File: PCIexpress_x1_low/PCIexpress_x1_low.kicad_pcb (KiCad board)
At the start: 6 copper layers, 167.7 x 68.9 mm, 29 parts, among them J1 PCIexpress_bracket, J2 PCIexpress_x1, J3 87832-1420, J4 PMOD_Host_Conn_02x06, J5 PMOD_Host_Conn_02x06, J6 PMOD_Host_Conn_02x06, U1 XC7A50T-CSG325, U2 LTM4643EY_PBF, U3 MX25L3233FM1

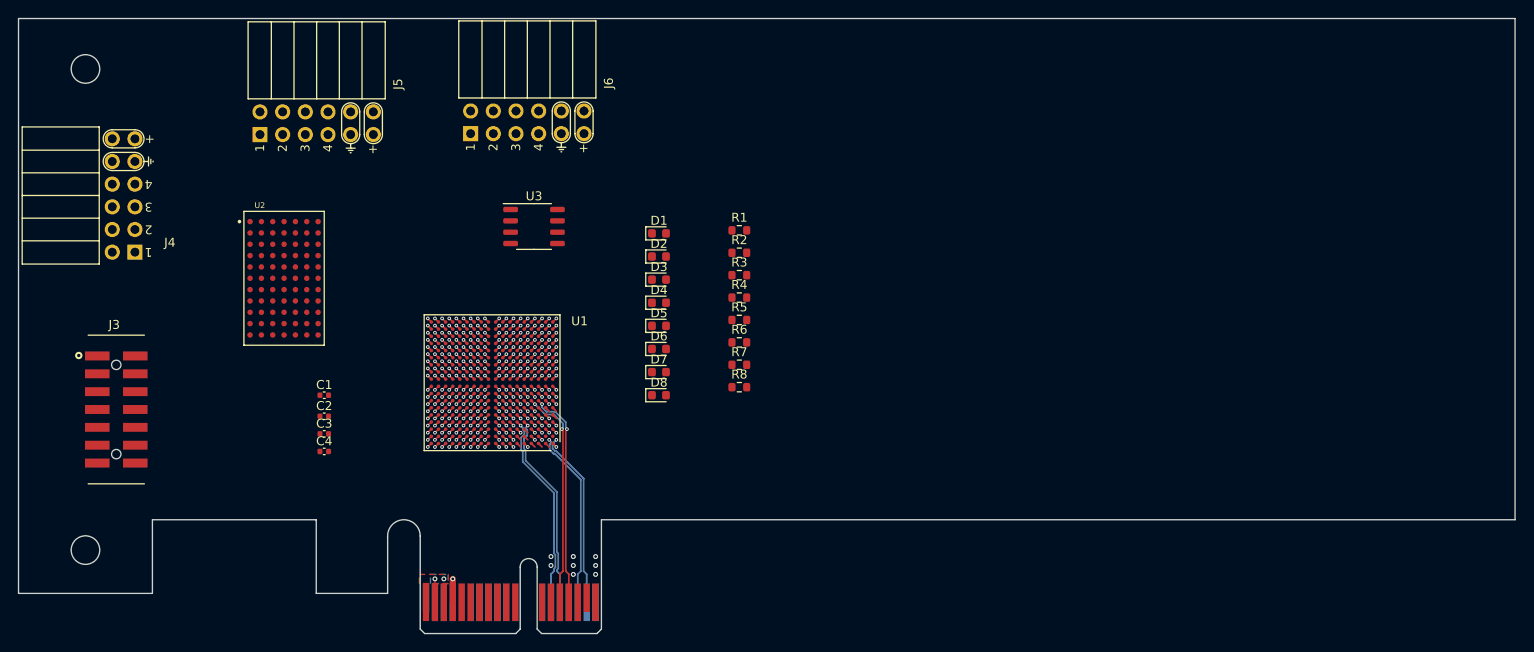
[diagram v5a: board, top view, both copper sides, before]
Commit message: using hierarchal sheets
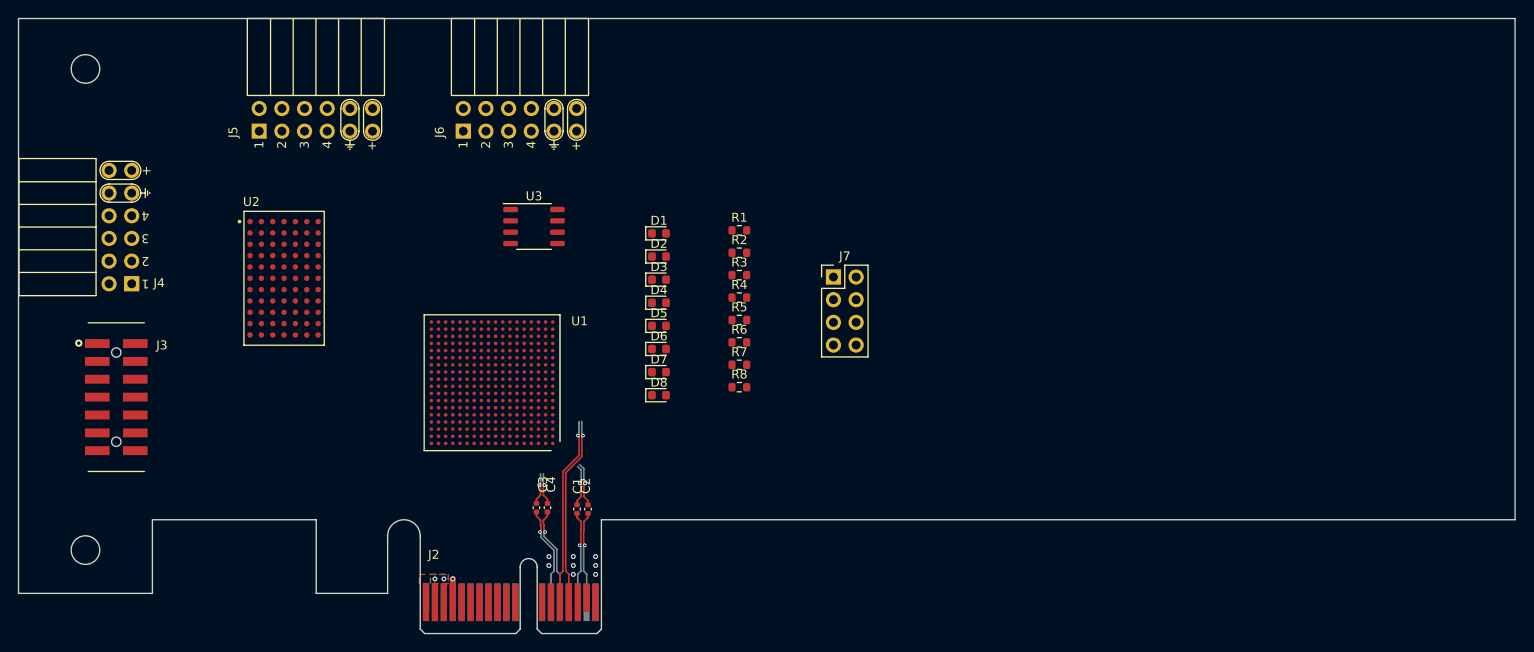
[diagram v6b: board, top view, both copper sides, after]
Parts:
- added J7: Conn_02x04_Odd_Even, Connector_PinHeader_2.54mm:PinHeader_2x04_P2.54mm_Vertical, F.Cu at (155.8, 154.2)
- C1, C2, C3, C4: value C -> 0.22uf
- moved C2 31.3 mm to (128.3, 180.2), turned to 90 degrees
- moved C1 31.1 mm to (127.0, 180.2), turned to 90 degrees
- moved C4 25.8 mm to (123.7, 180.0), turned to 90 degrees
- moved C3 25.2 mm to (122.5, 180.0), turned to 90 degrees
- moved J4 3.56 mm to (77.2, 154.9)
- moved J3 1.39 mm to (75.4, 167.6)
- moved J6 0.87 mm to (114.3, 137.8)
- moved J5 0.39 mm to (91.4, 137.8)
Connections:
- net /prsntn renamed /pcie/prsnt_n
- net /waken renamed /pcie/wake_n
- C1 pad 1: unconnected-(C1-Pad1) -> /pcie/REFCLK+
- C1 pad 2: unconnected-(C1-Pad2) -> /pcie/REFCLK_AC+
- C2 pad 1: unconnected-(C2-Pad1) -> /pcie/REFCLK-
- C2 pad 2: unconnected-(C2-Pad2) -> /pcie/REFCLK_AC-
- C3 pad 1: unconnected-(C3-Pad1) -> /pcie/PER0_P
- C3 pad 2: unconnected-(C3-Pad2) -> /pcie/PRE_PER0_P
- C4 pad 1: unconnected-(C4-Pad1) -> /pcie/PER0_N
- C4 pad 2: unconnected-(C4-Pad2) -> /pcie/PRE_PER0_N
- J2 pad A11: /perstn -> unconnected-(J2-~{PERST}-PadA11)
- J2 pad A13: /REFCLK+ -> /pcie/REFCLK+
- J2 pad A14: /REFCLK- -> /pcie/REFCLK-
- J2 pad A16: /PET0_P -> /pcie/PER0_P
- J2 pad A17: /PET0_N -> /pcie/PER0_N
- J2 pad B14: /PER0_P -> /pcie/PET0_P
- J2 pad B15: /PER0_N -> /pcie/PET0_N
- J4 pad 11: unconnected-(J4-GND-Pad11) -> GND
- J4 pad 12: unconnected-(J4-VCC-Pad12) -> +3V3
- J4 pad 5: unconnected-(J4-GND-Pad5) -> GND
- J4 pad 6: unconnected-(J4-VCC-Pad6) -> +3V3
- J5 pad 11: unconnected-(J5-GND-Pad11) -> GND
- J5 pad 12: unconnected-(J5-VCC-Pad12) -> +3V3
- J5 pad 5: unconnected-(J5-GND-Pad5) -> GND
- J5 pad 6: unconnected-(J5-VCC-Pad6) -> +3V3
- J6 pad 11: unconnected-(J6-GND-Pad11) -> GND
- J6 pad 12: unconnected-(J6-VCC-Pad12) -> +3V3
- J6 pad 5: unconnected-(J6-GND-Pad5) -> GND
- J6 pad 6: unconnected-(J6-VCC-Pad6) -> +3V3
- U1 pad B1: /PER0_N -> /fpga/PRE_PER0_N
- U1 pad B2: /PER0_P -> /fpga/PRE_PER0_P
- U1 pad D5: /REFCLK- -> /fpga/REFCLK_AC-
- U1 pad D6: /REFCLK+ -> /fpga/REFCLK_AC+
- U1 pad G3: /PET0_N -> /fpga/PET0_N
- U1 pad G4: /PET0_P -> /fpga/PET0_P
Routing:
- net /PET0_P: track 44.9 -> 0.00 mm, vias 3 -> 0
- net /PET0_N: track 44.7 -> 0.00 mm, vias 3 -> 0
- net (no net): track 0.00 -> 43.2 mm, vias 1 -> 5
- net GND: track 45.1 -> 2.62 mm, vias 84 -> 9
- net /REFCLK+: track 22.5 -> 0.00 mm, vias 1 -> 0
- net /REFCLK-: track 22.5 -> 0.00 mm, vias 1 -> 0
- net /pcie/PET0_N: track 0.00 -> 21.3 mm, vias 0 -> 1
- net /pcie/PET0_P: track 0.00 -> 21.3 mm, vias 0 -> 1
- net /pcie/REFCLK_AC-: track 0.00 -> 5.02 mm, vias 0 -> 1
- net /pcie/REFCLK_AC+: track 0.00 -> 4.76 mm, vias 0 -> 1
- net /pcie/PRE_PER0_N: track 0.00 -> 3.62 mm, vias 0 -> 1
- net /pcie/PRE_PER0_P: track 0.00 -> 3.62 mm, vias 0 -> 1
- net unconnected-(U1F-VCCINT-PadP9): track 0.57 -> 0.00 mm, vias 1 -> 0
- net unconnected-(U1F-VCCINT-PadP11): track 0.57 -> 0.00 mm, vias 1 -> 0
- net unconnected-(U1F-VCCINT-PadN8): track 0.57 -> 0.00 mm, vias 1 -> 0
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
